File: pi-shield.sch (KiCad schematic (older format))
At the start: 18 parts

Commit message: Progressing on pi shield
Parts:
- removed H? (x4): M3, symbol Mechanical:MountingHole
- removed U??: TLC59116, symbol pi-shield:TLC59116
- added BT?: 3V, symbol Device:Battery_Cell
- added C? (x2): 100n, symbol Device:C_Small
- added D?: LED, symbol Device:LED
- added H? (x4): M2, symbol Mechanical:MountingHole_Pad
- added J?: 0530470210, symbol Connector_Generic:Conn_01x02
- added J?: Conn_01x07, symbol Connector_Generic:Conn_01x07
- added J?: Conn_01x04, symbol Connector_Generic:Conn_01x04
- added J?: Conn_01x05, symbol Connector_Generic:Conn_01x05
- added R?: 10k, symbol Device:R_Small
- added R?: R_Small, symbol Device:R_Small
- added SW?: DIP SPST 100MA 6V, symbol Switch:SW_DIP_x01
- added U?: PCA9685BS, Package_DFN_QFN:QFN-28-1EP_6x6mm_P0.65mm_EP4.25x4.25mm, symbol Driver_LED:PCA9685BS
- added U?: DS3231, symbol pi-shield:DS3231
- J?: value Conn_01x14 -> 0530471410; descr (none) -> Front panel; digikey# (none) -> WM17004-ND
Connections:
- net labels added: +3.3V, +BATT, CS0, CS1, LCD_RS, LCD_RST, LED_BOARD, MISO, MOSI, ROBOT_SELECT, SCLK, SHDN_OK, SHDN_REQ, TS_INT
- wire segments 83 -> 189
- no-connect marks 7 -> 23
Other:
- note added: "TODO:\n* Alimentation Vbat -> 5V 3A pour le Pi\n* pick GPIOs on connector"
- note added: "i2c addr: 0x55\n"
- note added: "intended fan: MF20100V2-1000U-A99"
- note added: "touch module\naddr: 0x40\n"
- note removed: "TODO: Ca ne fonctionne pas, il faut à 3.3v\n"
- note removed: "TODO: Check fan mounting hole size\n"
- note removed: "TODO:\n* Alimentation Vbat -> 5V 3A pour le Pi\n* Drive les LEDs du front panel\n* Connecteur écran SPI / touch I2C\n* Robot select dip switch\n* Console UART\n* ventilateur intégré -> alimentation\n* Power control pins (shutdown request / shutdown ok)\n* Realtime Clock\n"
- moved on the sheet: C?, J?, JP?, U?

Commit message: Work on some other parts
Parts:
- added H5, H6, H7, H8: M2.5, MountingHole:MountingHole_2.7mm_M2.5_Pad_Via, symbol Mechanical:MountingHole_Pad
- added J10: Conn_01x04, Connector_Molex:Molex_PicoBlade_53048-0410_1x04_P1.25mm_Horizontal, symbol Connector_Generic:Conn_01x04
- added J9: Conn_01x04, Connector_Molex:Molex_PicoBlade_53261-0471_1x04-1MP_P1.25mm_Horizontal, symbol Connector_Generic:Conn_01x04
- C1, C2, C3, C4, C5, C6: renamed from C?; footprint (none) -> Capacitor_SMD:C_0805_2012Metric_Pad1.15x1.40mm_HandSolder
- D1: renamed from D?; footprint (none) -> LED_SMD:LED_0805_2012Metric_Pad1.15x1.40mm_HandSolder
- H1, H2, H3, H4: renamed from H?; footprint (none) -> MountingHole:MountingHole_2.5mm_Pad_Via
- J1: renamed from J?; footprint (none) -> Connector_PinSocket_2.54mm:PinSocket_2x20_P2.54mm_Vertical
- J2, J3: renamed from J?; footprint (none) -> Connector_Molex:Molex_PicoBlade_53047-0410_1x04_P1.25mm_Vertical
- J4: renamed from J?; footprint (none) -> Connector_Molex:Molex_PicoBlade_53047-0210_1x02_P1.25mm_Vertical
- J5: renamed from J?; footprint (none) -> Connector_Molex:Molex_PicoBlade_53048-0510_1x05_P1.25mm_Horizontal
- J6: renamed from J?; footprint (none) -> Connector_Molex:Molex_PicoBlade_53048-0710_1x07_P1.25mm_Horizontal
- J7: renamed from J?; footprint (none) -> Connector_Molex:Molex_PicoBlade_53048-1410_1x14_P1.25mm_Horizontal
- J8: renamed from J?; footprint (none) -> Connector_Molex:Molex_PicoBlade_53261-0471_1x04-1MP_P1.25mm_Horizontal
- JP1: renamed from JP?; footprint (none) -> Jumper:SolderJumper-2_P1.3mm_Open_RoundedPad1.0x1.5mm
- R1, R2, R3: renamed from R?; footprint (none) -> Resistor_SMD:R_0805_2012Metric_Pad1.15x1.40mm_HandSolder
- SW1: renamed from SW?; footprint (none) -> Button_Switch_SMD:SW_DIP_SPSTx01_Slide_Copal_CHS-01B_W7.62mm_P1.27mm
- U2: renamed from U?; footprint (none) -> Package_TO_SOT_SMD:SOT-23-8_Handsoldering
- U3: renamed from U?; footprint (none) -> Package_SO:SOIC-16W_7.5x12.8mm_P1.27mm
- gave numbers to parts that had none: 4
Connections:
- net +5V: now also JP1.2; no longer JP1.1
- net GND: now also H5.1, H6.1, H7.1, H8.1, J10.2 (Pin_2), J9.2 (Pin_2)
- net LED_BOARD: now also U4.16 (LED12); no longer U4.13 (LED9)
- net CANL: now reaches J2.4 (Pin_4), J3.4 (Pin_4), U2.6 (CANL)
- net CANL: now also J10.4 (Pin_4), J9.4 (Pin_4)
- net CANH: now reaches J2.3 (Pin_3), J3.3 (Pin_3), U2.7 (CANH)
- net CANH: now also J10.3 (Pin_3), J9.3 (Pin_3)
- net VBUS: now reaches J2.1 (Pin_1), J3.1 (Pin_1)
- net VBUS: now also JP1.1, J10.1 (Pin_1), J9.1 (Pin_1); no longer JP1.2
- no-connect marks 23 -> 24
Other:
- note added: "Horizontal\n\n\n"
- note added: "Vertical"
- moved on the sheet: BT1, C1, C2, C3, C4, C5, H1, H2, H3, H4, J2, J3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

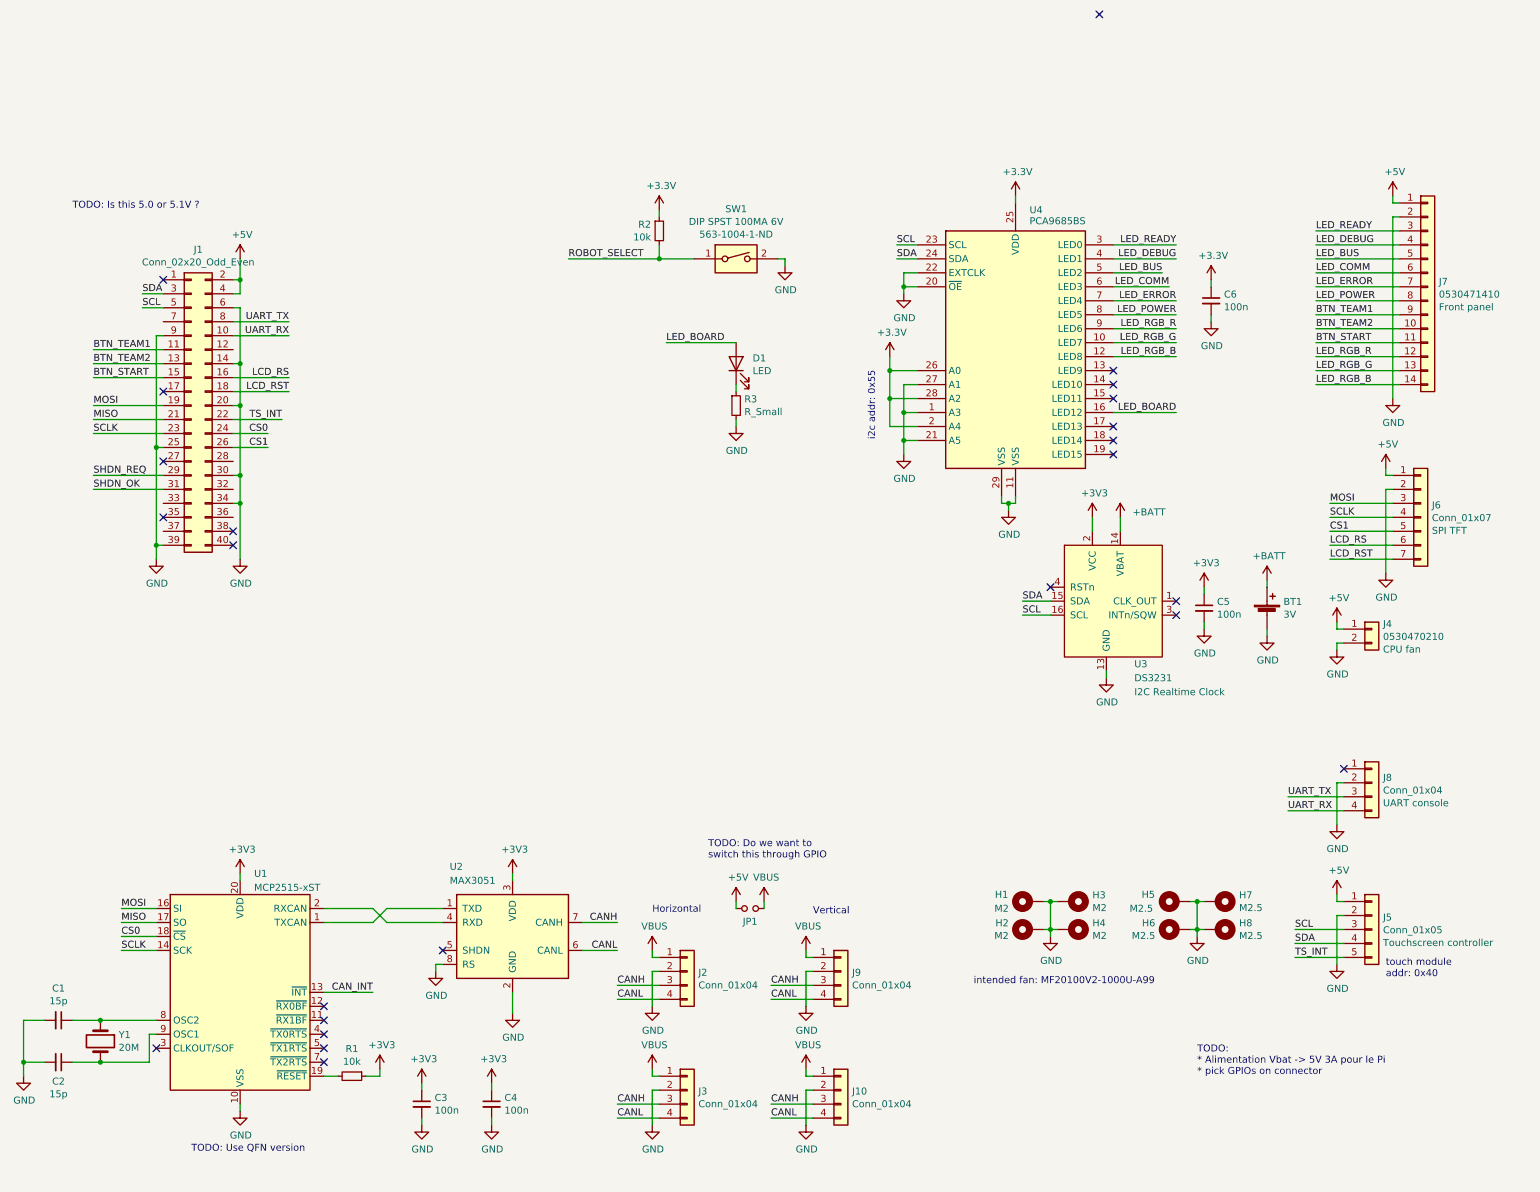
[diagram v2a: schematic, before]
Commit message: Progress on schematic and board outline
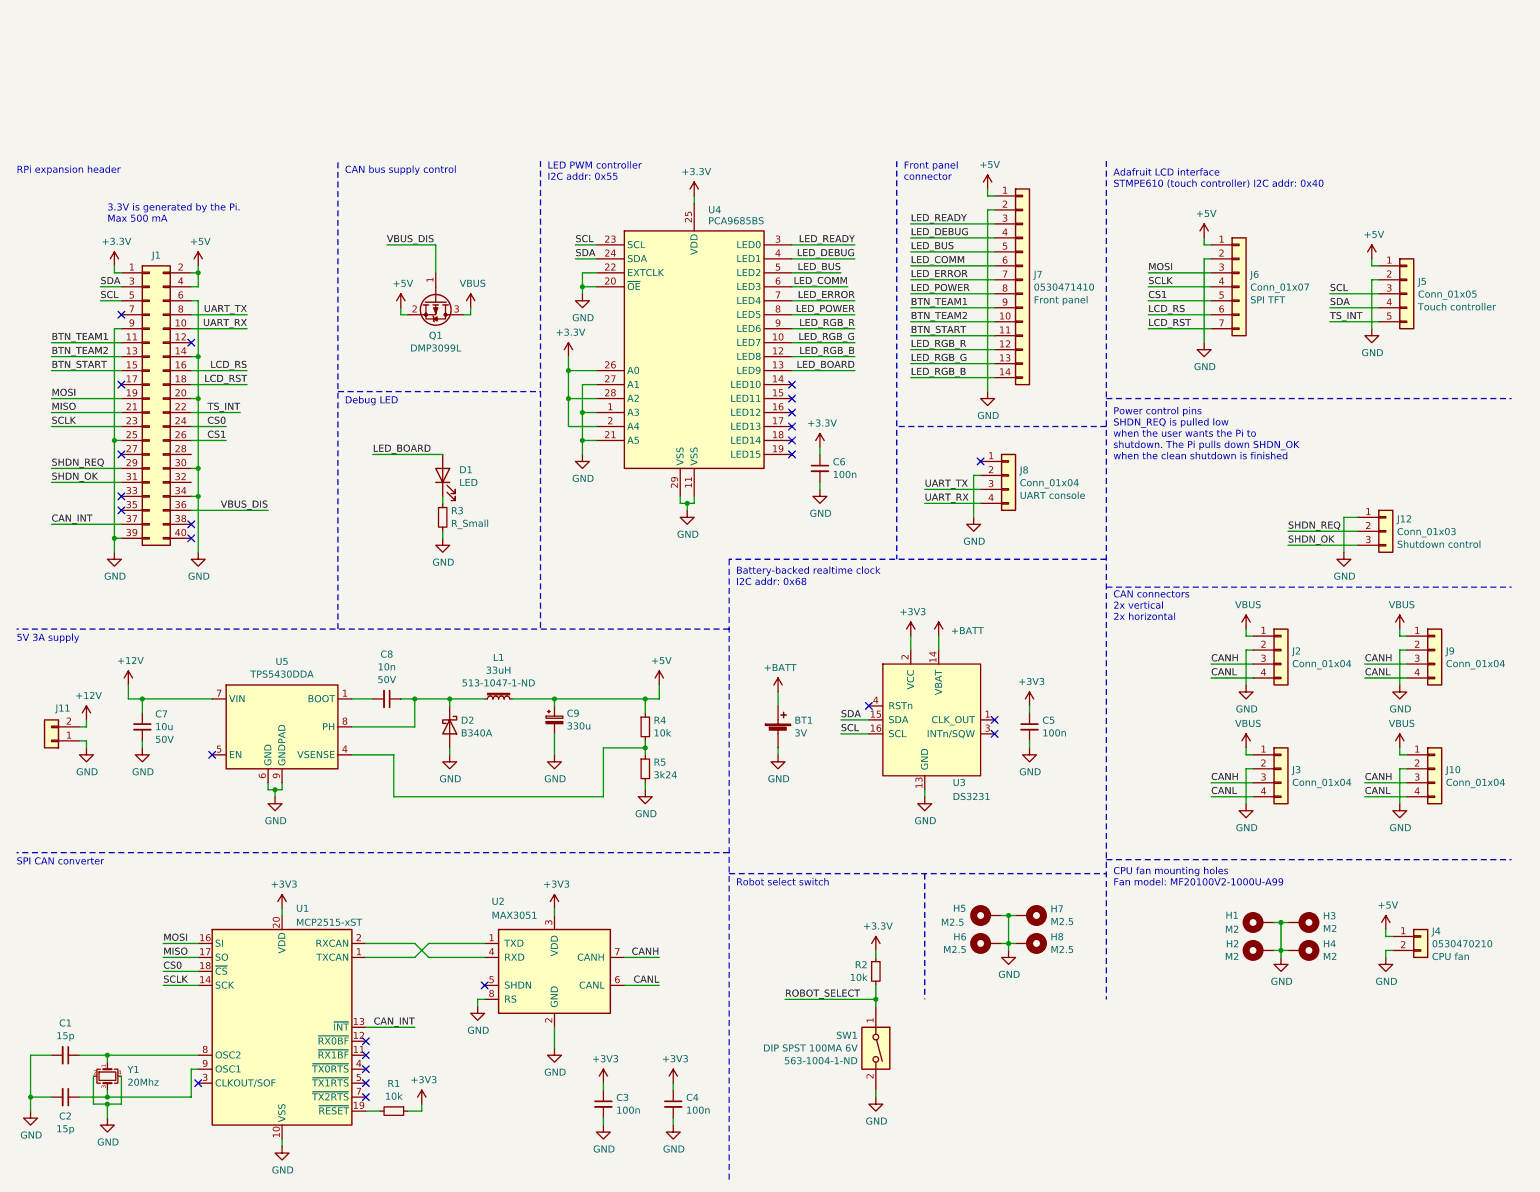
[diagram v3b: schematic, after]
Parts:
- removed JP1: Jumper_NO_Small, Jumper:SolderJumper-2_P1.3mm_Open_RoundedPad1.0x1.5mm, symbol Device:Jumper_NO_Small
- removed Y1: 20M, symbol Device:Crystal
- added C7: 10u, Capacitor_SMD:C_2220_5650Metric_Pad1.97x5.40mm_HandSolder, symbol Device:C_Small
- added C8: 10n, Capacitor_SMD:C_0603_1608Metric_Pad1.05x0.95mm_HandSolder, symbol Device:C_Small
- added C9: 330u, Capacitor_Tantalum_SMD:CP_EIA-7343-30_AVX-N_Pad2.25x2.55mm_HandSolder, symbol Device:CP_Small
- added D2: B340A, Diode_SMD:D_SMA, symbol Device:D_Schottky
- added J11: a, symbol Connector_Generic:Conn_01x02
- added J12: Conn_01x03, Connector_Molex:Molex_PicoBlade_53398-0471_1x04-1MP_P1.25mm_Vertical, symbol Connector_Generic:Conn_01x03
- added L1: 33uH, symbol Device:L_Core_Iron_Small
- added Q1: DMP3099L, Package_TO_SOT_SMD:SOT-23, symbol Device:Q_PMOS_GSD
- added R4: 10k, Resistor_SMD:R_0805_2012Metric, symbol Device:R_Small
- added R5: 3k24, Resistor_SMD:R_0805_2012Metric, symbol Device:R_Small
- added U5: TPS5430DDA, Package_SO:TI_SO-PowerPAD-8_ThermalVias, symbol Regulator_Switching:TPS5430DDA
- added Y1: 20Mhz, Crystal:Crystal_SMD_Abracon_ABM3C-4Pin_5.0x3.2mm, symbol Device:Crystal_GND24_Small
- J5: descr Touchscreen controller -> Touch controller
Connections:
- net +3V3: now also J1.1 (Pin_1)
- net +5V: now also C9.1, L1.2, Q1.2 (S), R4.1
- net CAN_INT: now also J1.37 (Pin_37)
- net GND: now also C7.2, C9.2, D2.2 (A), J11.1 (Pin_1), J12.1 (Pin_1), R5.2, U5.6 (GND), U5.9 (GNDPAD), Y1.2, Y1.4
- net LED_BOARD: now also U4.13 (LED9); no longer U4.16 (LED12)
- net SHDN_OK: now also J12.3 (Pin_3)
- net SHDN_REQ: now also J12.2 (Pin_2)
- net VBUS: now also Q1.3 (D)
- net VBUS_DIS: now reaches J1.36 (Pin_36)
- net VBUS_DIS: now also Q1.1 (G)
- net at C1.1, U1.8 (OSC2): now also Y1.1
- net at C2.1, U1.9 (OSC1): now also Y1.3
- new net: C8.2, U5.1 (BOOT)
- new net: R4.2, R5.1, U5.4 (VSENSE)
- new net: C8.1, D2.1 (K), L1.1, U5.8 (PH)
- new net +12V: C7.1, J11.2 (Pin_2), U5.7 (VIN)
- no-connect marks 24 -> 26
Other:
- note added: "3.3V is generated by the Pi.\nMax 500 mA"
- note added: "5V 3A supply"
- note added: "Adafruit LCD interface\nSTMPE610 (touch controller) I2C addr: 0x40"
- note added: "Battery-backed realtime clock\nI2C addr: 0x68\n"
- note added: "CAN bus supply control\n"
- note added: "CAN connectors\n2x vertical\n2x horizontal"
- note added: "CPU fan mounting holes\nFan model: MF20100V2-1000U-A99"
- note added: "Debug LED\n"
- note added: "Front panel\nconnector\n"
- note added: "LED PWM controller\nI2C addr: 0x55"
- note added: "Power control pins\nSHDN_REQ is pulled low\nwhen the user wants the Pi to\nshutdown. The Pi pulls down SHDN_OK\nwhen the clean shutdown is finished"
- note added: "RPi expansion header"
- note added: "Robot select switch"
- note added: "SPI CAN converter"
- note removed: "Horizontal\n\n\n"
- note removed: "TODO: Do we want to\nswitch this through GPIO"
- note removed: "TODO: Is this 5.0 or 5.1V ?"
- note removed: "TODO: Use QFN version\n"
- note removed: "TODO:\n* Alimentation Vbat -> 5V 3A pour le Pi\n* pick GPIOs on connector"
- note removed: "Vertical"
- note removed: "i2c addr: 0x55\n"
- note removed: "intended fan: MF20100V2-1000U-A99"
- note removed: "touch module\naddr: 0x40\n"
- moved on the sheet: BT1, C1, C2, C3, C4, C5, C6, D1, H1, H2, H3, H4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
